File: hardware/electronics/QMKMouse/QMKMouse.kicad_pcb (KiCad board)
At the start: 4 copper layers, 104.6 x 65.8 mm, 117 parts

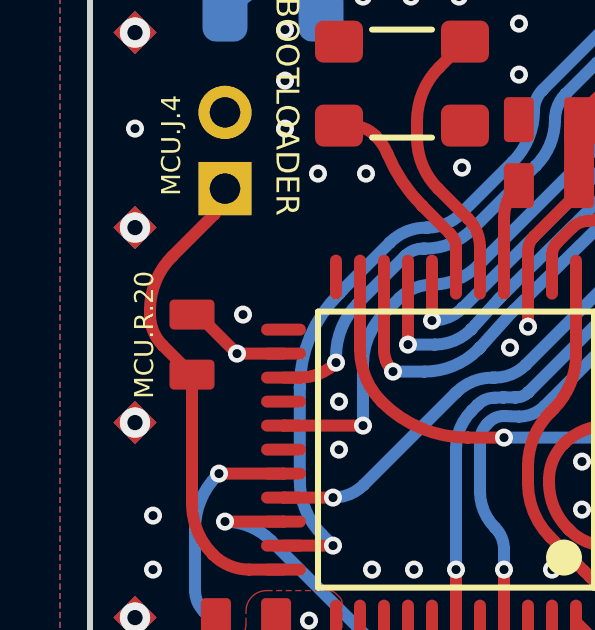
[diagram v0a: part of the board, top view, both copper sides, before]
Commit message: import 0805 footprint into its own library to allow assignment of 3d model
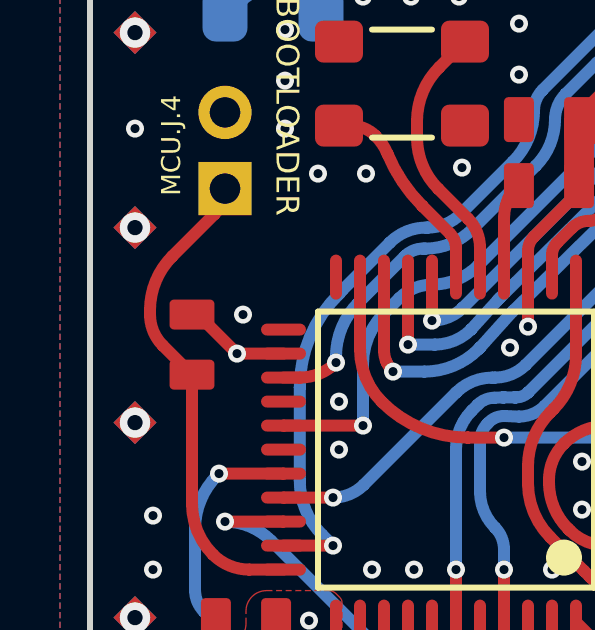
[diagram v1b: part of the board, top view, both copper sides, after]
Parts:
- LED.C.20, LED.C.21, LED.C.23, LED.C.24, LED.C.25, LED.C.26, LED.C.27, LED.C.28, LED.R.16, LED.R.17, LED.R.18, LED.R.19, MCU.C.1, MCU.C.22, MCU.C.4, MCU.C.5, MCU.C.6, MCU.C.7, MCU.C.8, MCU.C.9, MCU.R.1, MCU.R.20, MOS.C.10, MOS.C.11, MOS.R.3, MOS.R.4, MOS.R.5, REG.C.12, REG.C.13, REG.C.14, REG.C.15, REG.C.16, REG.C.17, REG.C.18, SCW.R.1, SCW.R.2, SCW.R.3, SCW.R.4, USB.C.19, USB.FB.1, USB.FB.2, USB.FB.3, USB.FB.4, USB.FB.5, USB.R.10, USB.R.11, USB.R.12, USB.R.13, USB.R.14, USB.R.15, USB.R.6, USB.R.7, USB.R.8, USB.R.9: footprint Chip_Passives.PcbLib:0805 -> mouse_part:0805

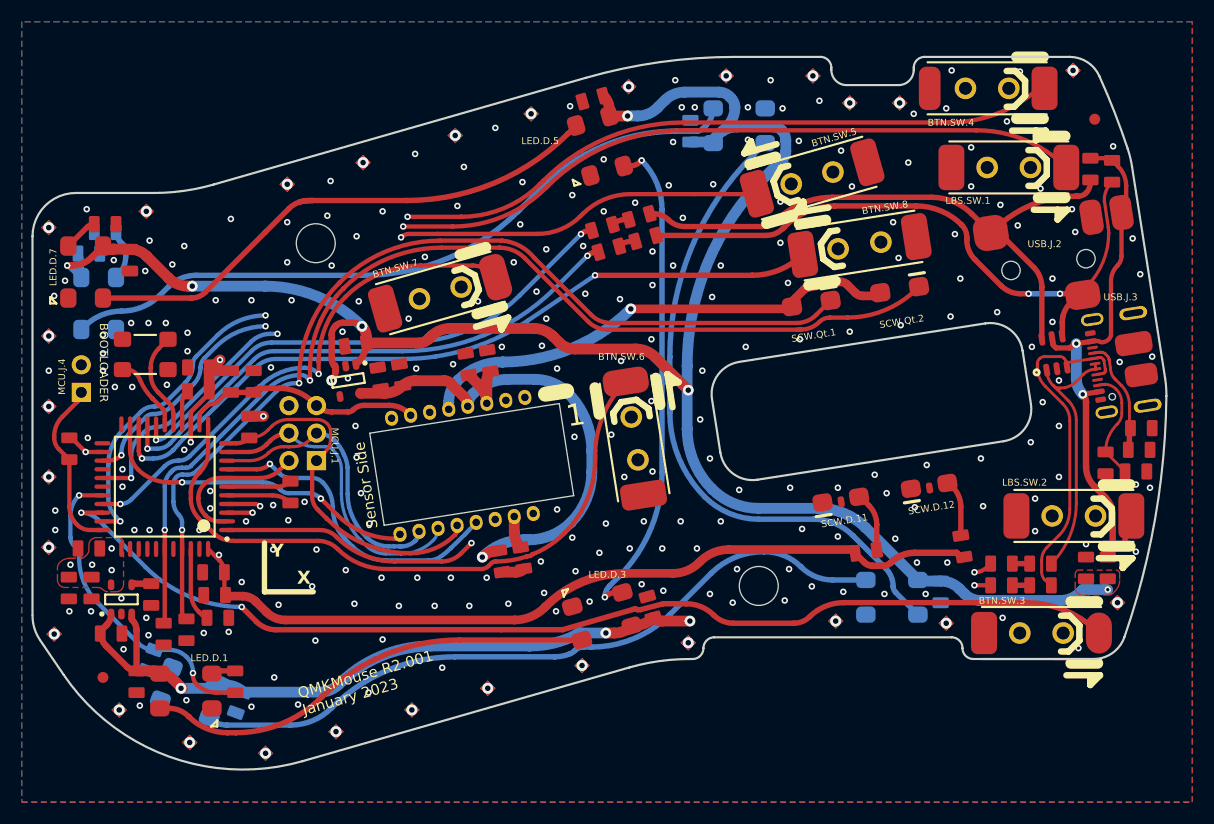
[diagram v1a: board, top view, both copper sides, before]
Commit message: reference 3d model to all components
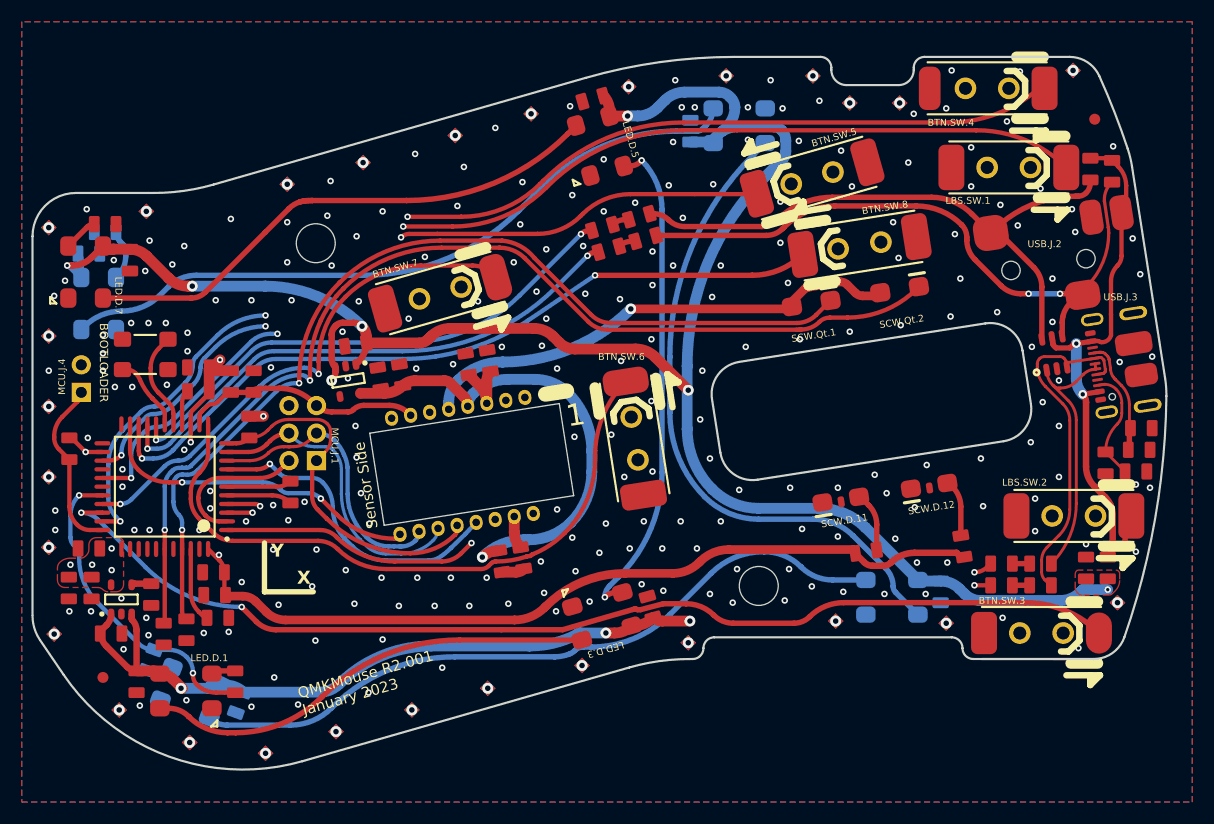
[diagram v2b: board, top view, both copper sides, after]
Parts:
- LED.C.20, LED.C.21, LED.C.23, LED.C.24, LED.C.25, LED.C.26, LED.C.27, LED.C.28, MCU.C.1, MCU.C.22, MCU.C.4, MCU.C.5, MCU.C.6, MCU.C.7, MCU.C.8, MCU.C.9, MOS.C.10, MOS.C.11, REG.C.12, REG.C.13, REG.C.14, REG.C.15, REG.C.16, REG.C.17, REG.C.18, USB.C.19: footprint mouse_part:0805 -> mouse_part:C_0805
- LED.D.1, LED.D.2, LED.D.3, LED.D.4, LED.D.5, LED.D.6, LED.D.7, LED.D.8: footprint LEDs.PcbLib:IN-PI55TATPRPGPB -> mouse_part:IN-PI55TATPRPGPB
- turned REG.U.4 to -81.113 degrees
- turned USB.Z.1 to 98.887 degrees
